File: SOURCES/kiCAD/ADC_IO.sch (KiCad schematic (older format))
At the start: 155 parts, among them IC2 PCM1808QPWRQ1, J1 Conn_01x08, J10 Conn_01x02, J11 Conn_Coaxial, J12 IDC_2x5, J3 Conn_01x08, J5 MJ-519, J6 8P_DIP_SOCKET, J9 Conn_01x02, Q12 MJD45H11T4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

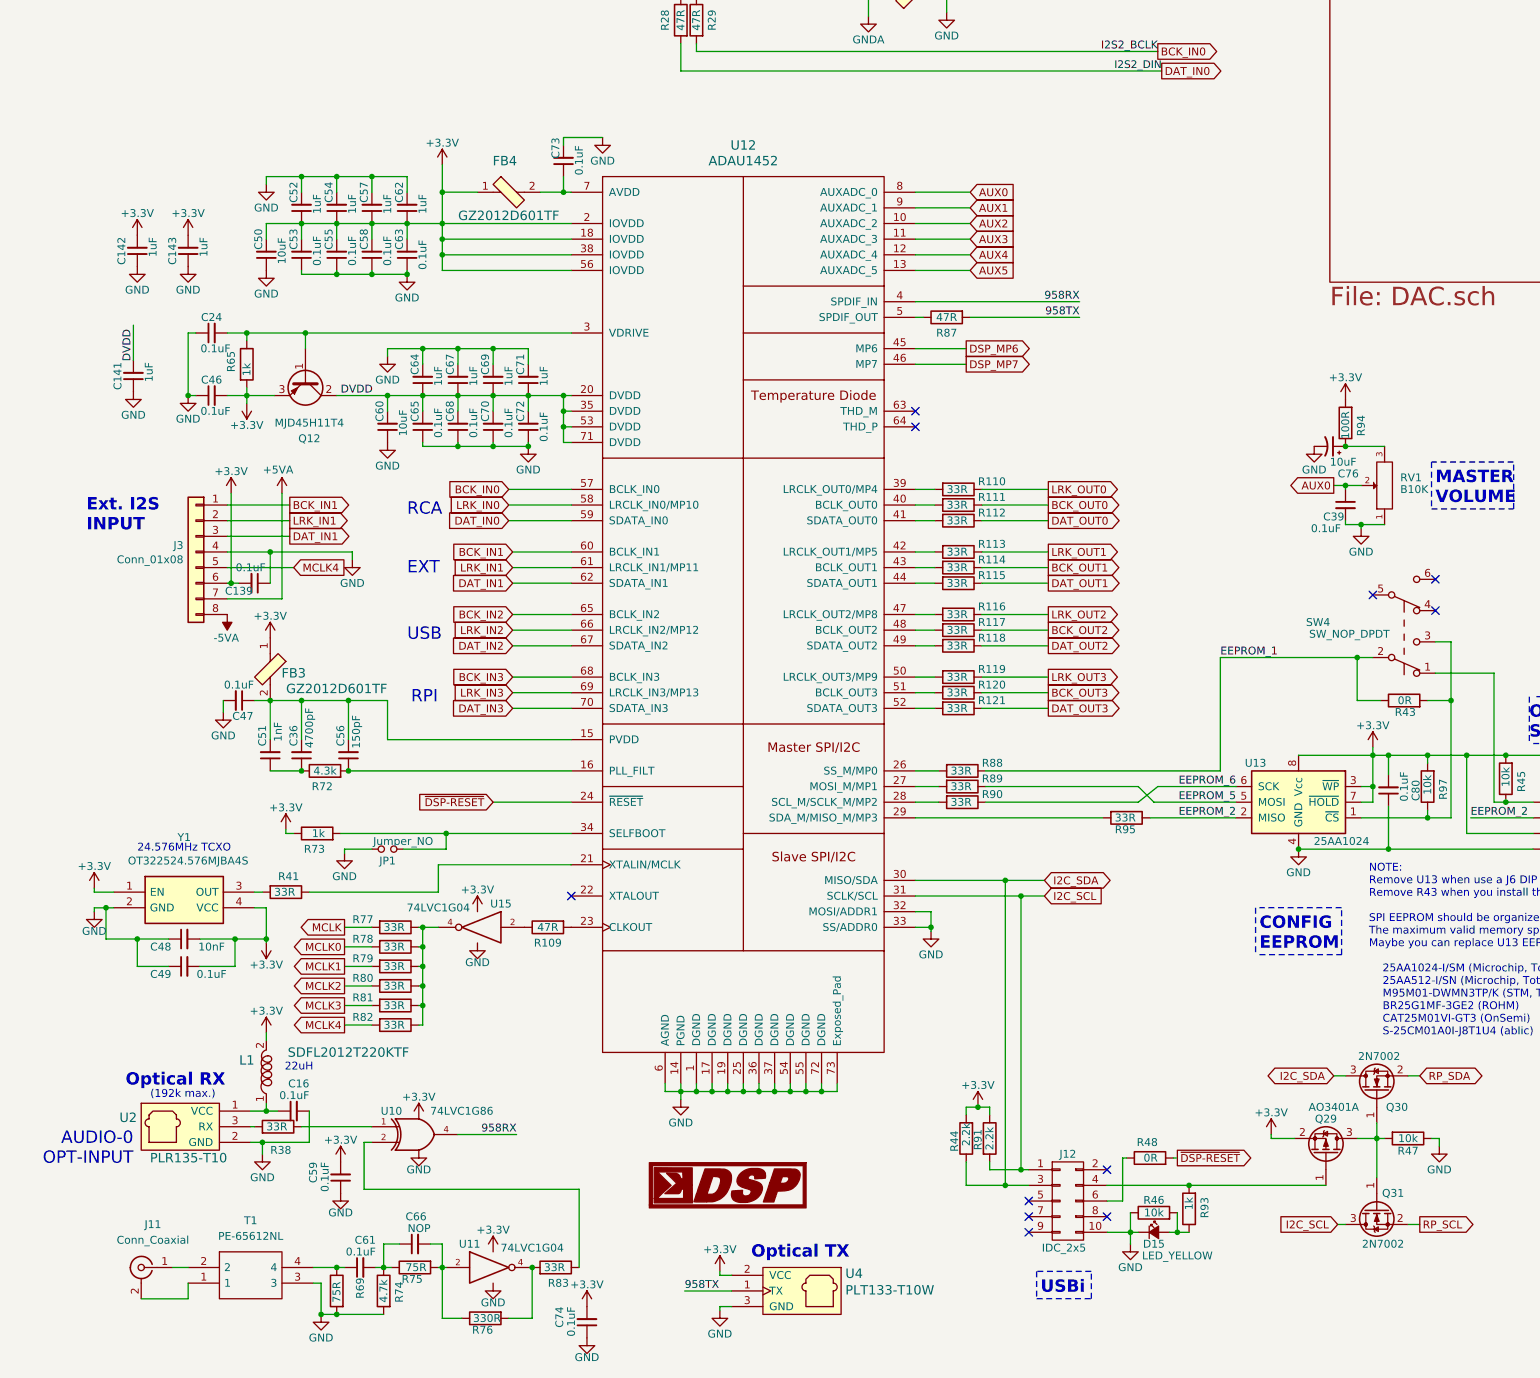
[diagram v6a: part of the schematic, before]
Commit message: Improved Coax Input Noise Immunities
Changed Coax input amp design and AC couling to EXOR
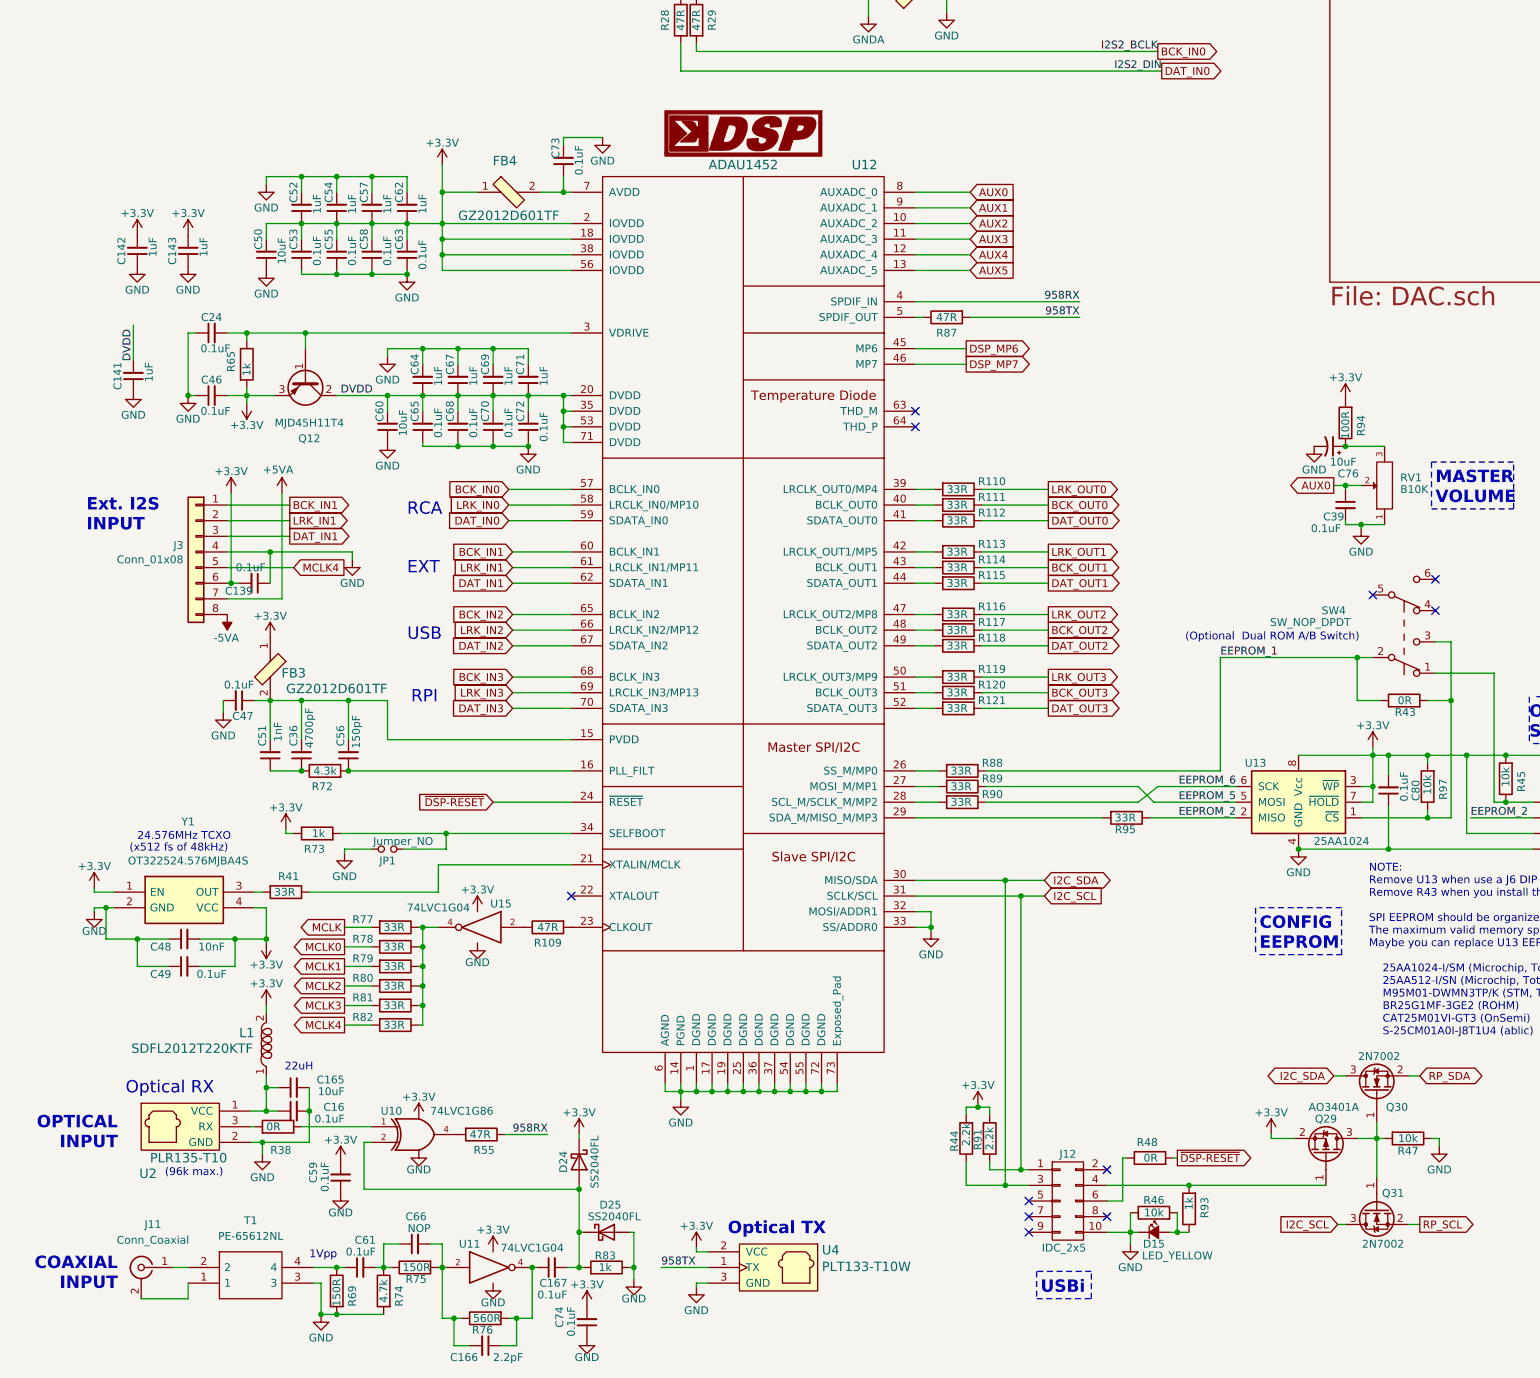
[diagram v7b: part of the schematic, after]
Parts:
- added C165: 10uF, Capacitor_SMD:C_0603_1608Metric, symbol Device:C_Small
- added C166: 2.2pF, Capacitor_SMD:C_0402_1005Metric_Pad0.74x0.62mm_HandSolder, symbol Device:C_Small
- added C167: 0.1uF, Capacitor_SMD:C_0603_1608Metric, symbol Device:C_Small
- added D24, D25: SS2040FL, Diode_SMD:D_SOD-123, symbol Diode:BAT43W-V
- added R55: 47R, Resistor_SMD:R_0603_1608Metric, symbol Device:R
- R38: value 33R -> 0R; JLPCB# C23140 -> C21189
- R69, R75: value 75R -> 150R; JLPCB# C4275 -> C22808
- R76: value 330R -> 560R; JLPCB# C17630 -> C23204
- R83: value 33R -> 1k; JLPCB# C23140 -> C21190
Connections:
- net +3V3: now also D24.1 (K)
- net 958RX: now also R55.1; no longer U10.4
- net GND: now also R83.1, C165.2, D25.2 (A)
- net at C16.1, L1.1, U2.1 (VCC): now also C165.1
- net at C66.2, R75.2, R76.1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: now also C166.2
- net at R76.2, U11.4: now also C166.1, C167.1; no longer R83.2
- net at U10.2: now also R83.2, C167.2, D24.2 (A), D25.1 (K); no longer R83.1
- new net: R55.2, U10.4
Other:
- note added: "(96k max.)"
- note added: "(Optional Dual ROM A/B Switch)"
- note added: "(x512 fs of 48kHz)"
- note added: "1Vpp"
- note added: "COAXIAL\nINPUT"
- note added: "OPTICAL\nINPUT"
- note removed: "(192k max.)"
- note removed: "AUDIO-0\nOPT-INPUT"
- moved on the sheet: L1, R83, U4
